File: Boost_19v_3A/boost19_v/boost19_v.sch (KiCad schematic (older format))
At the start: 20 parts, among them J1 4P2C, J2 4P2C, U1 TPS55340QRTERQ1

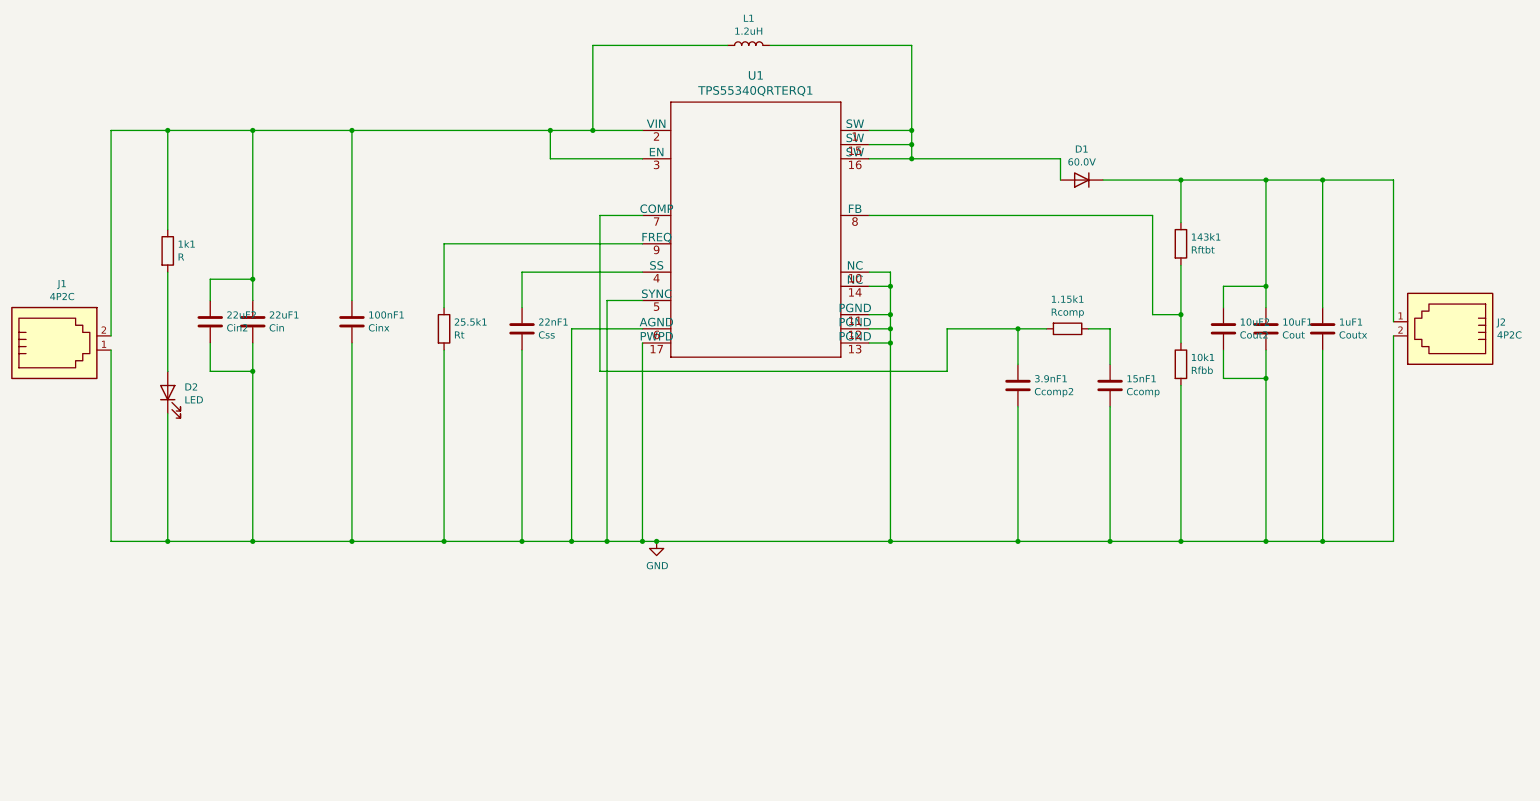
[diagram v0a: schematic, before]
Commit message: boost19v pcb layout updated
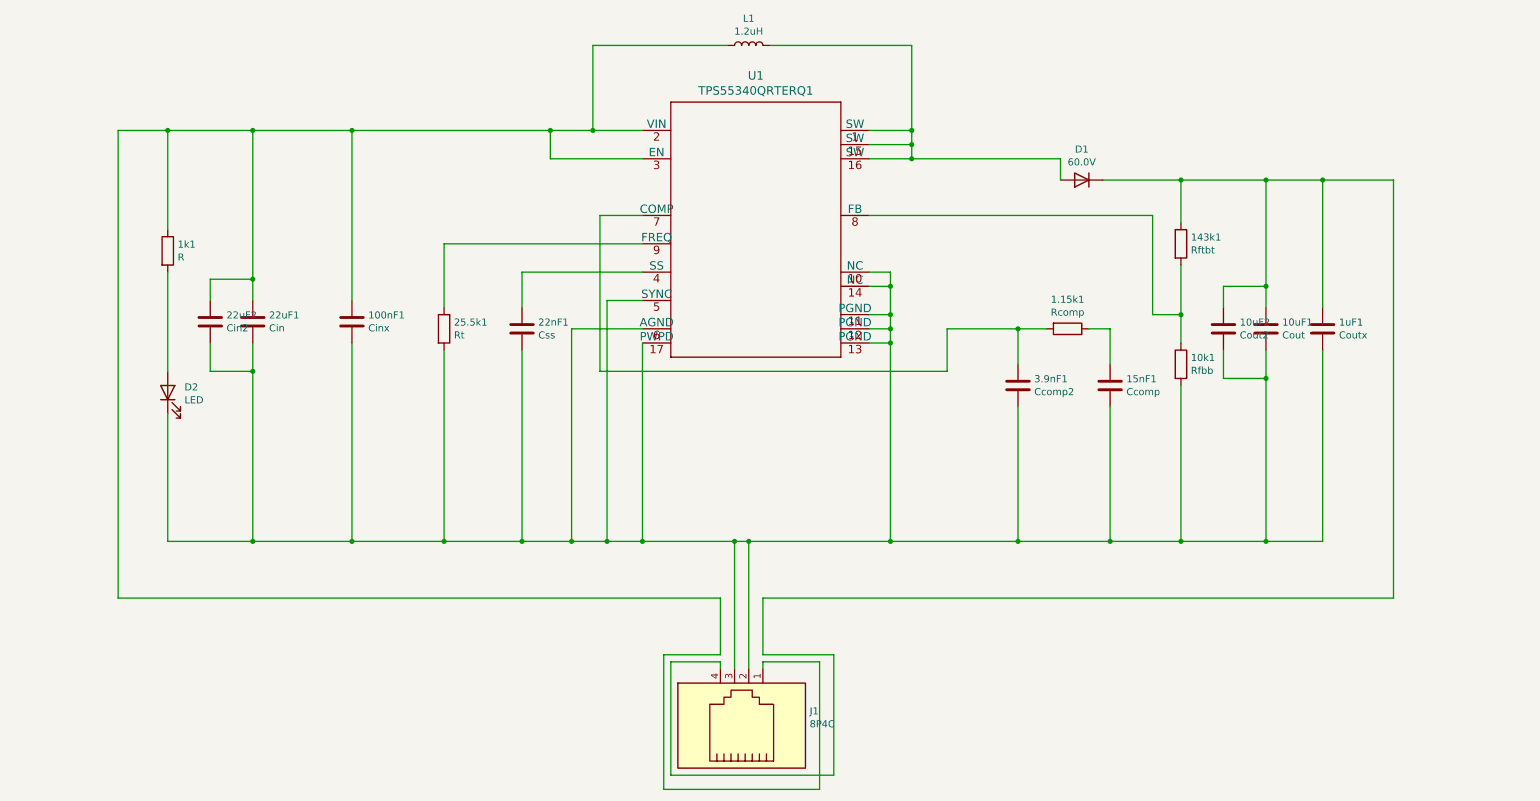
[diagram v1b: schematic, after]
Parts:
- removed J1, J2: 4P2C, 4p2c:43045-0200, symbol connector:4P2C
- added J1: 8P4C, 4x1_connector:436500400, symbol connector:8P4C
- U1: footprint IC:TPS55340QRTERQ1 -> IC_update:TPS55340QRTERQ1_002
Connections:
- net at 100nF1.1, 1k1.1, 22uF1.1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: now also J1.1
- net at 10uF1.1, 10uF2.1, 143k1.1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: now also J1.4
- net GND: no longer names the net of 100nF1.2, 10k1.2, 10uF1.2, 10uF2.2, 15nF1.2, 1uF1.2, 22nF1.2, 22uF1.2, 22uF2.2, 25.5k1.2, 3.9nF1.2, D2.1 (K), U1.10 (NC), U1.11 (PGND), U1.12 (PGND), U1.13 (PGND), U1.14 (NC), U1.17 (PWPD), U1.5 (SYNC), U1.6 (AGND)
- net GND: now also J1.2, J1.3
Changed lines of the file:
@@
 F 0 "U1" H 5900 3586 60  0000 C CNN
 F 1 "TPS55340QRTERQ1" H 5900 3480 60  0000 C CNN
-F 2 "IC:TPS55340QRTERQ1" H 5900 2440 60  0001 C CNN
+F 2 "IC_update:TPS55340QRTERQ1_002" H 5900 2440 60  0001 C CNN
 F 3 "" H 5900 2500 60  0000 C CNN
 	1    5900 2500
@@
 $EndComp
 Wire Wire Line
-	1350 1800 1350 3250
-Wire Wire Line
 	1750 2500 1750 1800
-Connection ~ 1750 1800
-Wire Wire Line
-	1750 1800 1350 1800
 Wire Wire Line
 	2350 3000 2350 2850
@@
 	3050 1800 4450 1800
 Wire Wire Line
-	1350 4700 1750 4700
-Wire Wire Line
-	10400 4700 10400 3250
-Wire Wire Line
 	3700 3050 3700 2600
 Wire Wire Line
@@
 Wire Wire Line
 	1750 3800 1750 4700
-Connection ~ 1750 4700
 Wire Wire Line
 	1750 4700 2350 4700
@@
 	8050 2000 8050 2150
 Wire Wire Line
-	10400 2150 10400 3150
-Wire Wire Line
 	9900 3050 9900 2150
 Connection ~ 9900 2150
@@
 Wire Wire Line
 	6850 4700 7750 4700
-Connection ~ 9900 4700
 Wire Wire Line
 	9500 3050 9500 2900
@@
 Wire Wire Line
 	9900 2150 10400 2150
-Wire Wire Line
-	9900 4700 10400 4700
 Connection ~ 8900 2150
 Wire Wire Line
@@
 	2350 3500 2350 4700
 Wire Wire Line
-	1350 3350 1350 4700
-$Comp
-L connector:4P2C J2
-U 1 1 6016D5C3
-P 10800 3150
-F 0 "J2" H 10470 3154 50  0000 R CNN
-F 1 "4P2C" H 10470 3245 50  0000 R CNN
-F 2 "4p2c:43045-0200" V 10800 3200 50  0001 C CNN
-F 3 "" V 10800 3200 50  0001 C CNN
-	1    10800 3150
-	-1   0    0    1
-$EndComp
-$Comp
-L connector:4P2C J1
-U 1 1 6016D4DD
-P 950 3350
-F 0 "J1" H 1005 3817 50  0000 C CNN
-F 1 "4P2C" H 1005 3726 50  0000 C CNN
-F 2 "4p2c:43045-0200" V 950 3400 50  0001 C CNN
-F 3 "" V 950 3400 50  0001 C CNN
-	1    950  3350
-	1    0    0    -1
-$EndComp
-$Comp
-L power:GND #PWR0101
-U 1 1 607312D8
-P 5200 4700
-F 0 "#PWR0101" H 5200 4450 50  0001 C CNN
-F 1 "GND" H 5205 4527 50  0000 C CNN
-F 2 "" H 5200 4700 50  0001 C CNN
-F 3 "" H 5200 4700 50  0001 C CNN
-	1    5200 4700
-	1    0    0    -1
-$EndComp
-Connection ~ 5200 4700
-Wire Wire Line
-	5200 4700 6850 4700
-Wire Wire Line
 	5100 3300 5100 4700
 Connection ~ 5100 4700
 Wire Wire Line
-	5100 4700 5200 4700
+	5100 4700 5750 4700
+$Comp
+L connector:8P4C J1
+U 1 1 60AEB758
+P 5850 6000
+F 0 "J1" V 5952 5570 50  0000 R CNN
+F 1 "8P4C" V 5861 5570 50  0000 R CNN
+F 2 "4x1_connector:436500400" V 5850 6025 50  0001 C CNN
+F 3 "" V 5850 6025 50  0001 C CNN
+	1    5850 6000
+	0    -1   -1   0
+$EndComp
+Connection ~ 5750 4700
+Wire Wire Line
+	5750 4700 5850 4700
+Connection ~ 5850 4700
+Wire Wire Line
+	5850 4700 6850 4700
+Wire Wire Line
+	1750 1800 1400 1800
+Wire Wire Line
+	1400 1800 1400 5100
+Wire Wire Line
+	1400 5100 5650 5100
+Wire Wire Line
+	5650 5100 5650 5500
+Connection ~ 1750 1800
+Wire Wire Line
+	10400 2150 10400 5100
+Wire Wire Line
+	10400 5100 5950 5100
+Wire Wire Line
+	5950 5100 5950 5500
+Wire Wire Line
+	5650 5500 5250 5500
+Wire Wire Line
+	5250 5500 5250 6450
+Wire Wire Line
+	5250 6450 6350 6450
+Wire Wire Line
+	6350 6450 6350 5550
+Wire Wire Line
+	6350 5550 5950 5550
+Wire Wire Line
+	5950 5550 5950 5600
+Wire Wire Line
+	5950 5500 6450 5500
+Wire Wire Line
+	6450 5500 6450 6350
+Wire Wire Line
+	6450 6350 5300 6350
+Wire Wire Line
+	5300 6350 5300 5550
+Wire Wire Line
+	5300 5550 5650 5550
+Wire Wire Line
+	5650 5550 5650 5600
+Wire Wire Line
+	5750 4700 5750 5600
+Wire Wire Line
+	5850 4700 5850 5600
 $EndSCHEMATC
